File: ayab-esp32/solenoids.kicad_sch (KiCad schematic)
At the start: 60 parts

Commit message: first draft schematic
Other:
- company: matei repair lab -> matei
- title: MECHANICAL INTERFACE -> SOLENOID DRIVERS

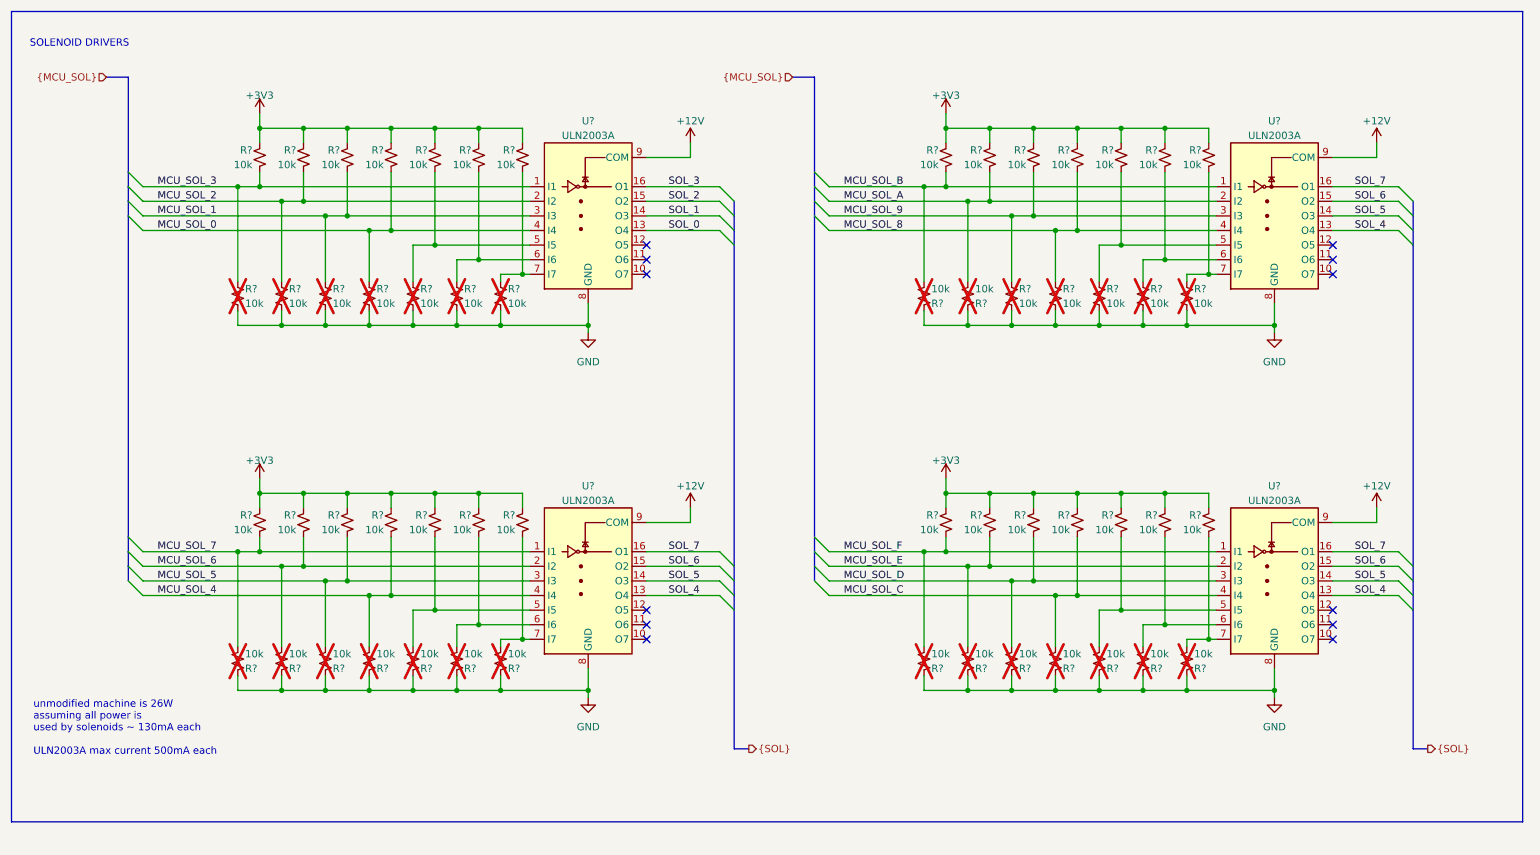
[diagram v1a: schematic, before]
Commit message: add capacitor on solenoid drivers
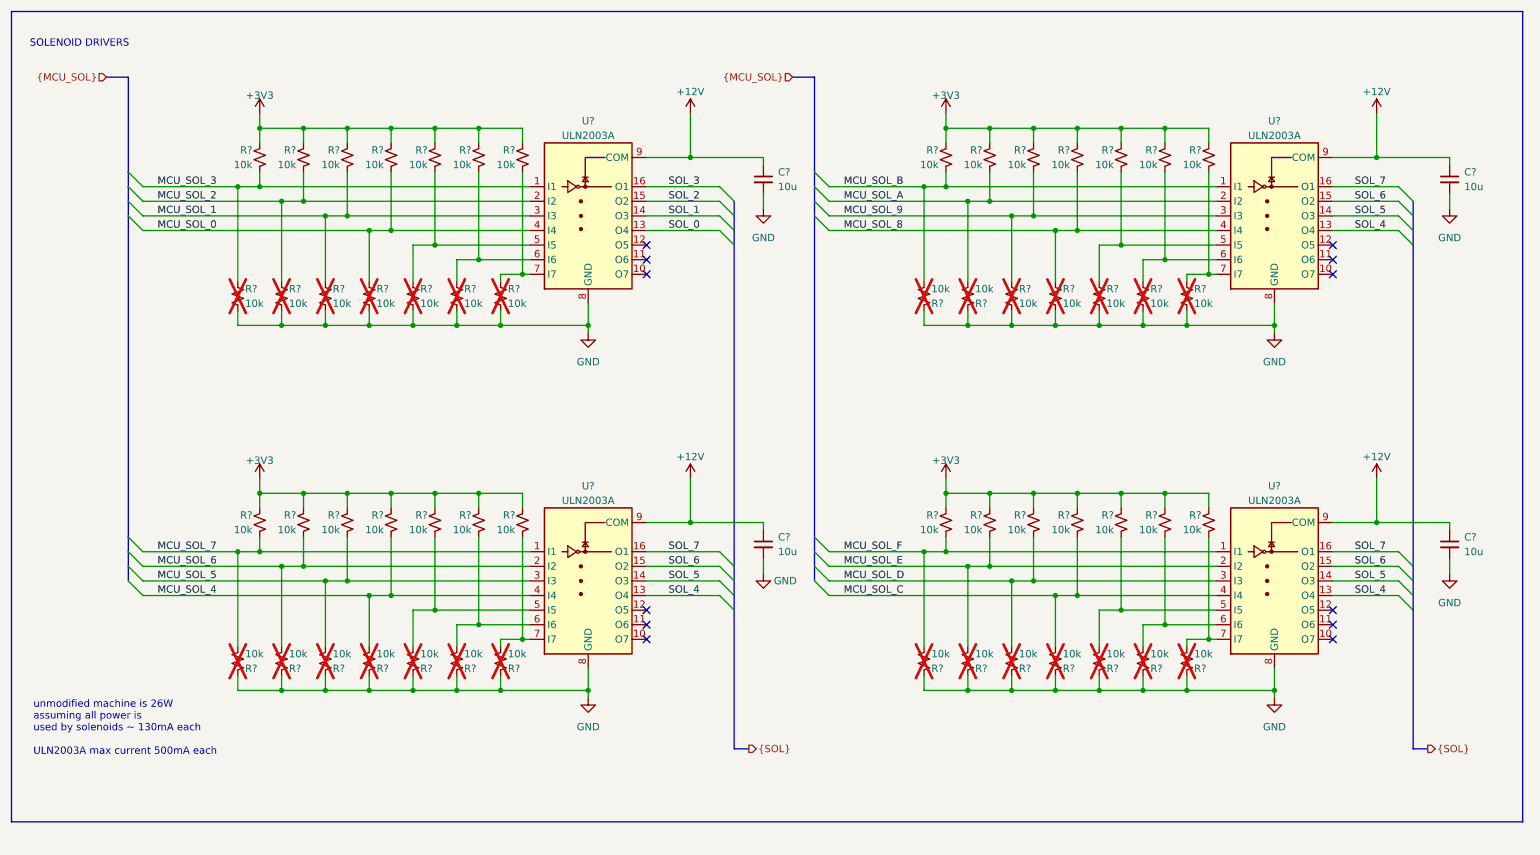
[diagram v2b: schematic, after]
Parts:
- added C? (x4): 10u, symbol Device:C_Small
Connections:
- net +12V: now also C?.1, C?.1, C?.1, C?.1
- net GND: now also C?.2, C?.2, C?.2, C?.2

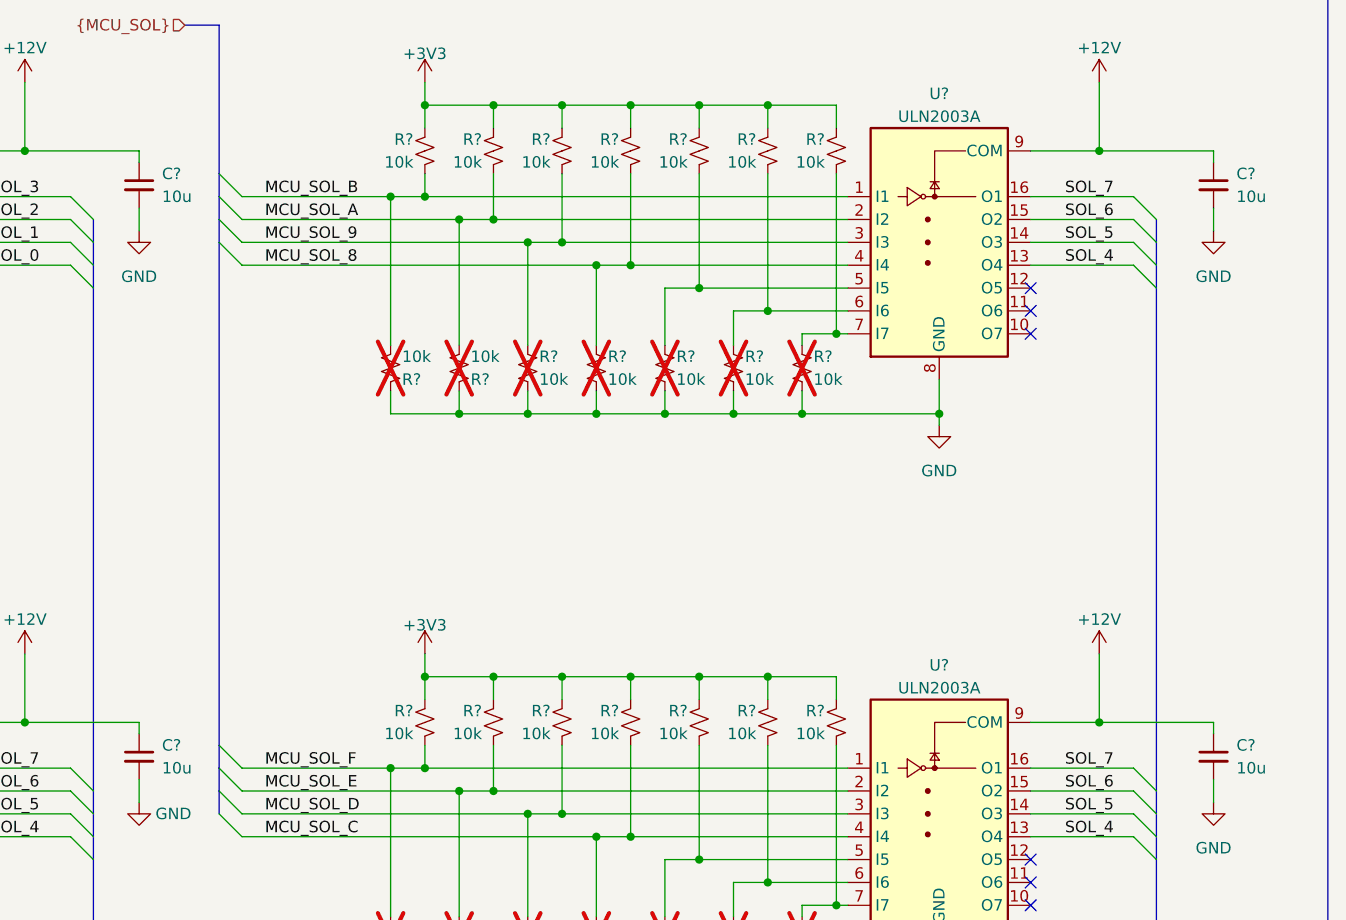
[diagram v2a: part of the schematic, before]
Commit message: add pch MOSFET for polarity protection
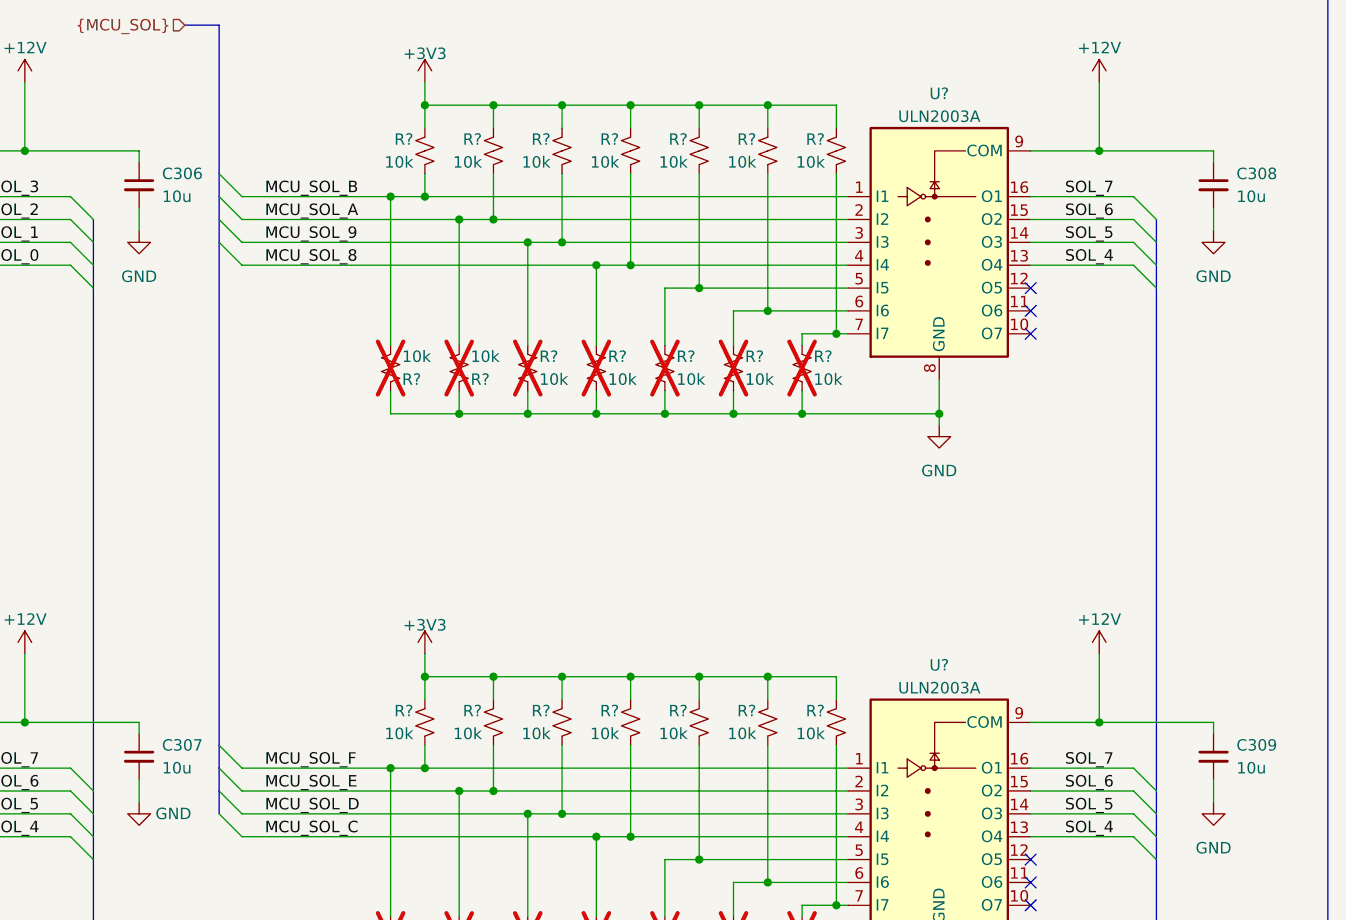
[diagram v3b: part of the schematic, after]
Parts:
- gave numbers to parts that had none: 4
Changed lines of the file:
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@@
   (symbol (lib_id "Device:C_Small") (at 267.97 45.72 0) (unit 1)
     (in_bom yes) (on_board yes) (dnp no)
-    (property "Reference" "C?" (at 270.51 44.4563 0)
+    (property "Reference" "C308" (at 270.51 44.4563 0)
       (effects (font (size 1.27 1.27)) (justify left))
     )
@@
       (project "ayab-esp32"
         (path "/ad16b75f-afc8-4717-a7c6-8dd7b69a18e2/5c12a608-dfd1-46fe-96db-4ec512a20774"
-          (reference "C?") (unit 1)
+          (reference "C308") (unit 1)
         )
       )
@@
   (symbol (lib_id "Device:C_Small") (at 148.59 45.72 0) (unit 1)
     (in_bom yes) (on_board yes) (dnp no)
-    (property "Reference" "C?" (at 151.13 44.4563 0)
+    (property "Reference" "C306" (at 151.13 44.4563 0)
       (effects (font (size 1.27 1.27)) (justify left))
     )
@@
       (project "ayab-esp32"
         (path "/ad16b75f-afc8-4717-a7c6-8dd7b69a18e2/5c12a608-dfd1-46fe-96db-4ec512a20774"
-          (reference "C?") (unit 1)
+          (reference "C306") (unit 1)
         )
       )
@@
   (symbol (lib_id "Device:C_Small") (at 148.59 109.22 0) (unit 1)
     (in_bom yes) (on_board yes) (dnp no)
-    (property "Reference" "C?" (at 151.13 107.9563 0)
+    (property "Reference" "C307" (at 151.13 107.9563 0)
       (effects (font (size 1.27 1.27)) (justify left))
     )
@@
       (project "ayab-esp32"
         (path "/ad16b75f-afc8-4717-a7c6-8dd7b69a18e2/5c12a608-dfd1-46fe-96db-4ec512a20774"
-          (reference "C?") (unit 1)
+          (reference "C307") (unit 1)
         )
       )
@@
   (symbol (lib_id "Device:C_Small") (at 267.97 109.22 0) (unit 1)
     (in_bom yes) (on_board yes) (dnp no)
-    (property "Reference" "C?" (at 270.51 107.9563 0)
+    (property "Reference" "C309" (at 270.51 107.9563 0)
       (effects (font (size 1.27 1.27)) (justify left))
     )
@@
       (project "ayab-esp32"
         (path "/ad16b75f-afc8-4717-a7c6-8dd7b69a18e2/5c12a608-dfd1-46fe-96db-4ec512a20774"
-          (reference "C?") (unit 1)
-        )
-      )
+          (reference "C309") (unit 1)
+        )
+      )

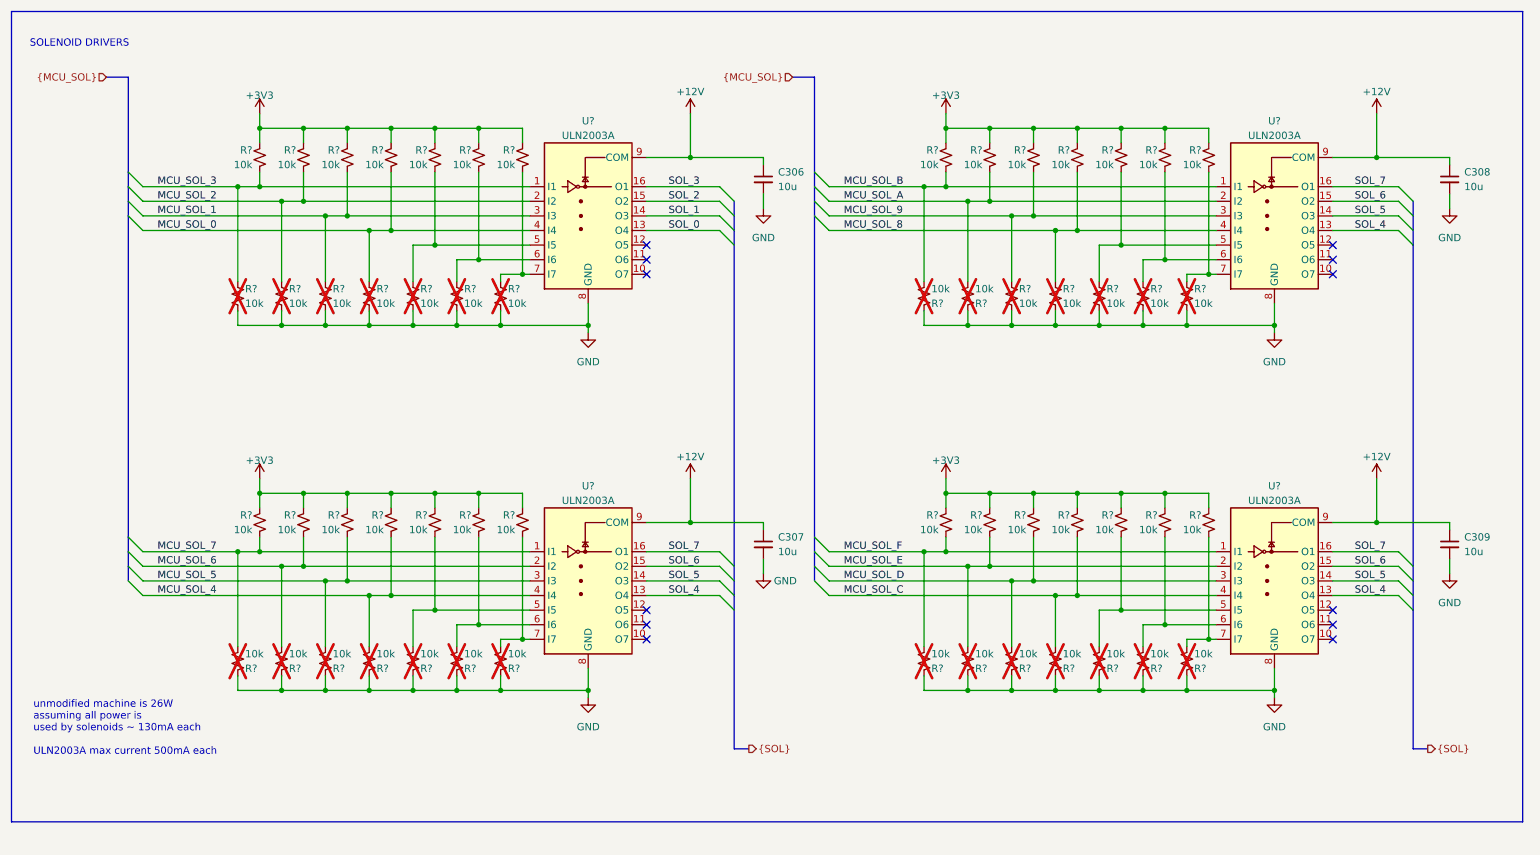
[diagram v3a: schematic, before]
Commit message: add ideal diode, remove extra uln2003a, add comparator for analog EOL sensors
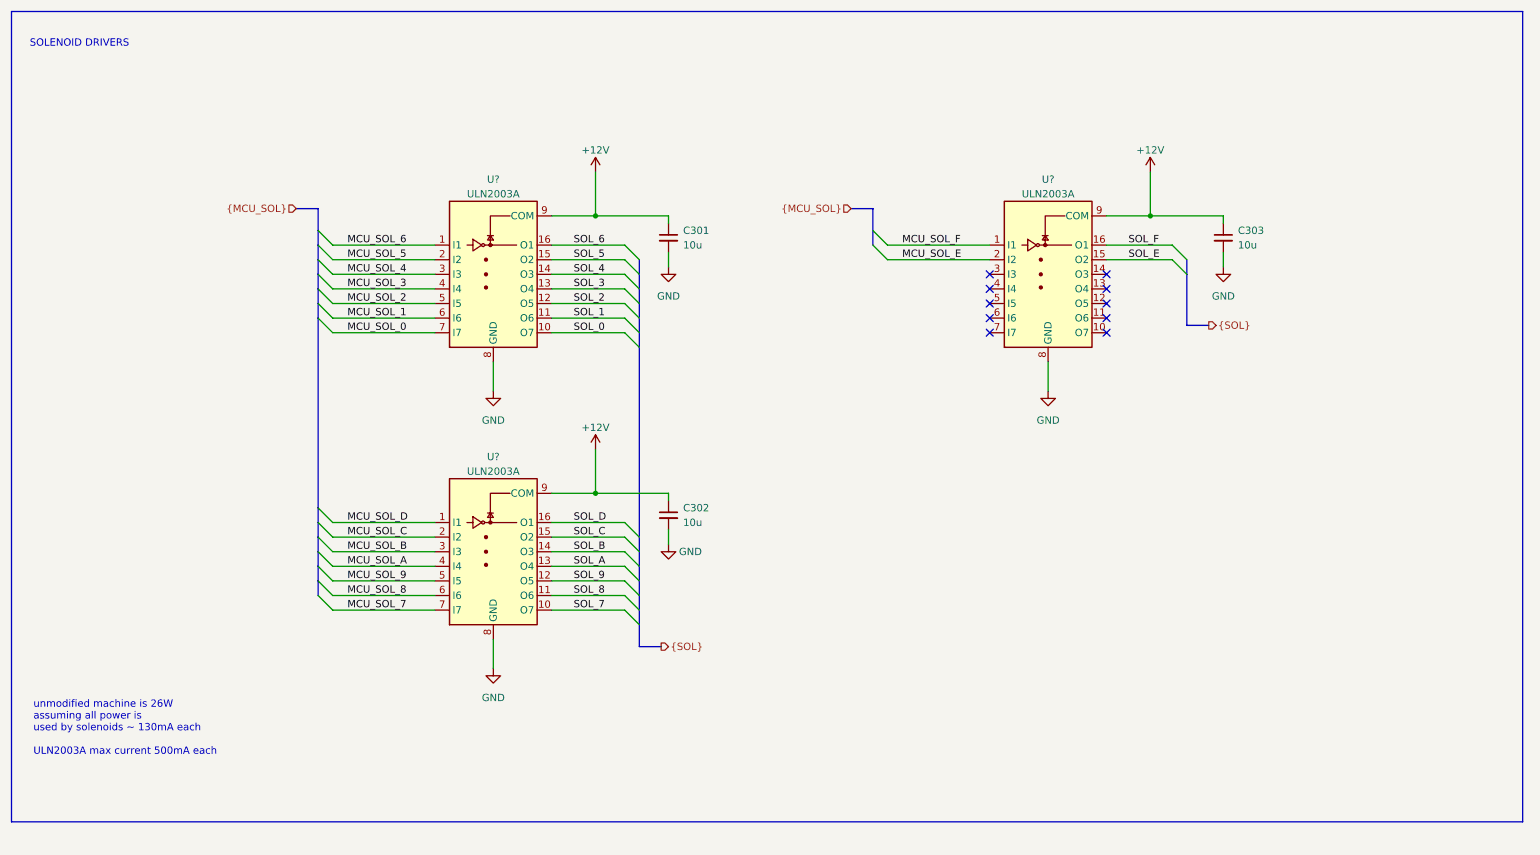
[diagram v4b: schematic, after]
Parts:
- removed C309: 10u, symbol Device:C_Small
- removed R? (x56): 10k, Resistor_SMD:R_0603_1608Metric, symbol Device:R_Small_US
- removed U?: ULN2003A, Package_SO:SOIC-16_3.9x9.9mm_P1.27mm, symbol Transistor_Array:ULN2003A
- renumbered C306 to C301, C307 to C302, C308 to C303
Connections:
- net MCU_SOL_0: now also U?.7 (I7); no longer U?.4 (I4)
- net MCU_SOL_1: now also U?.6 (I6); no longer U?.3 (I3)
- net MCU_SOL_2: now also U?.5 (I5); no longer U?.2 (I2)
- net MCU_SOL_3: now also U?.4 (I4); no longer U?.1 (I1)
- net MCU_SOL_4: now also U?.3 (I3); no longer U?.4 (I4)
- net MCU_SOL_5: now also U?.2 (I2); no longer U?.3 (I3)
- net MCU_SOL_6: now also U?.1 (I1); no longer U?.2 (I2)
- net MCU_SOL_7: now also U?.7 (I7); no longer U?.1 (I1)
- net MCU_SOL_8: now also U?.6 (I6); no longer U?.4 (I4)
- net MCU_SOL_9: now also U?.5 (I5); no longer U?.3 (I3)
- net MCU_SOL_A: now also U?.4 (I4); no longer U?.2 (I2)
- net MCU_SOL_B: now also U?.3 (I3); no longer U?.1 (I1)
- net MCU_SOL_C: now also U?.2 (I2)
- net MCU_SOL_D: now also U?.1 (I1)
- net MCU_SOL_E: now also U?.2 (I2)
- net MCU_SOL_F: now also U?.1 (I1)
- net SOL_0: now also U?.10 (O7); no longer U?.13 (O4)
- net SOL_1: now also U?.11 (O6); no longer U?.14 (O3)
- net SOL_2: now also U?.12 (O5); no longer U?.15 (O2)
- net SOL_3: now also U?.13 (O4); no longer U?.16 (O1)
- net SOL_4: now also U?.14 (O3); no longer U?.13 (O4), U?.13 (O4)
- net SOL_5: now also U?.15 (O2); no longer U?.14 (O3), U?.14 (O3)
- net SOL_6: now also U?.16 (O1); no longer U?.15 (O2), U?.15 (O2)
- net SOL_7: now also U?.10 (O7); no longer U?.16 (O1), U?.16 (O1)
- net SOL_8: now reaches U?.11 (O6)
- net SOL_9: now reaches U?.12 (O5)
- new net SOL_A: U?.13 (O4)
- new net SOL_B: U?.14 (O3)
- new net SOL_C: U?.15 (O2)
- new net SOL_D: U?.16 (O1)
- new net SOL_E: U?.15 (O2)
- new net SOL_F: U?.16 (O1)
- no-connect marks 12 -> 10
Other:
- moved on the sheet: C301, C302, C303, U?

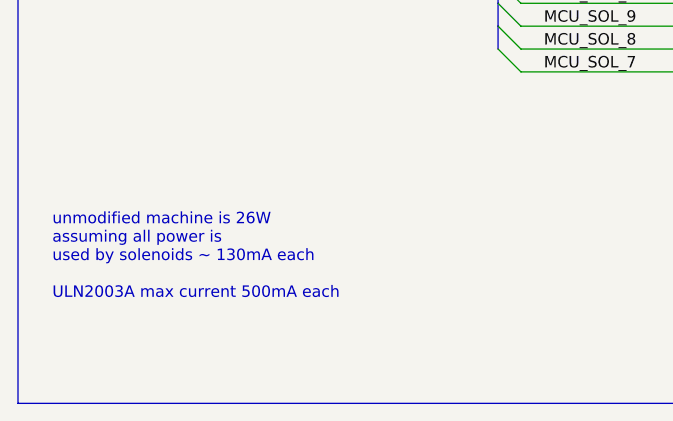
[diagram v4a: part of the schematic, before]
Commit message: fix comparator
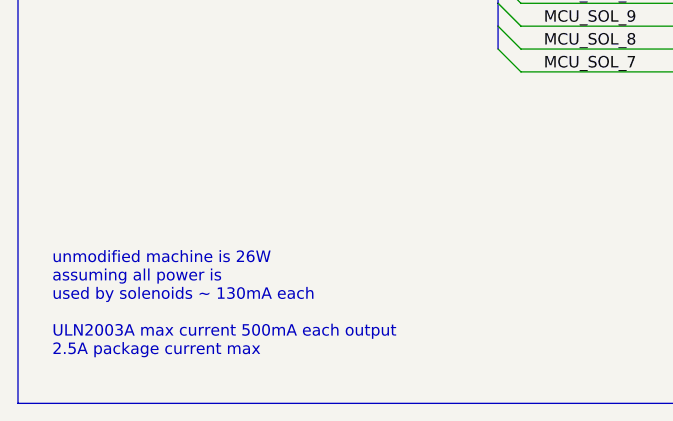
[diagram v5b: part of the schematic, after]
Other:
- note added: "unmodified machine is 26W assuming all power is used by solenoids ~ 130mA each ULN2003A max current 500mA each output 2.5A package current max"
- note removed: "unmodified machine is 26W assuming all power is used by solenoids ~ 130mA each ULN2003A max current 500mA each"
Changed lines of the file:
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@@
     (stroke (width 0) (type default))
   )
-  (text "unmodified machine is 26W\nassuming all power is \nused by solenoids ~ 130mA each\n\nULN2003A max current 500mA each\n"
-    (at 21.59 146.05 0)
+  (text "unmodified machine is 26W\nassuming all power is \nused by solenoids ~ 130mA each\n\nULN2003A max current 500mA each output\n2.5A package current max\n"
+    (at 21.59 152.4 0)
     (effects (font (size 1.27 1.27)) (justify left bottom))
   )
